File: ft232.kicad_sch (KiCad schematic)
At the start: 20 parts, among them J3 tp_ft232_, Q1 2N7002, U2 FT232BM

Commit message: Fix KiCad 10 footprint library: register kiC library, fix schematic references
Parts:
- J3: footprint Connector_Pin:pad_0508 -> kiC:pad_0508
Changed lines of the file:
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@@
 			)
 		)
-		(property "Footprint" "Connector_Pin:pad_0508"
+		(property "Footprint" "kiC:pad_0508"
 			(at 172.72 66.04 0)
 			(hide yes)

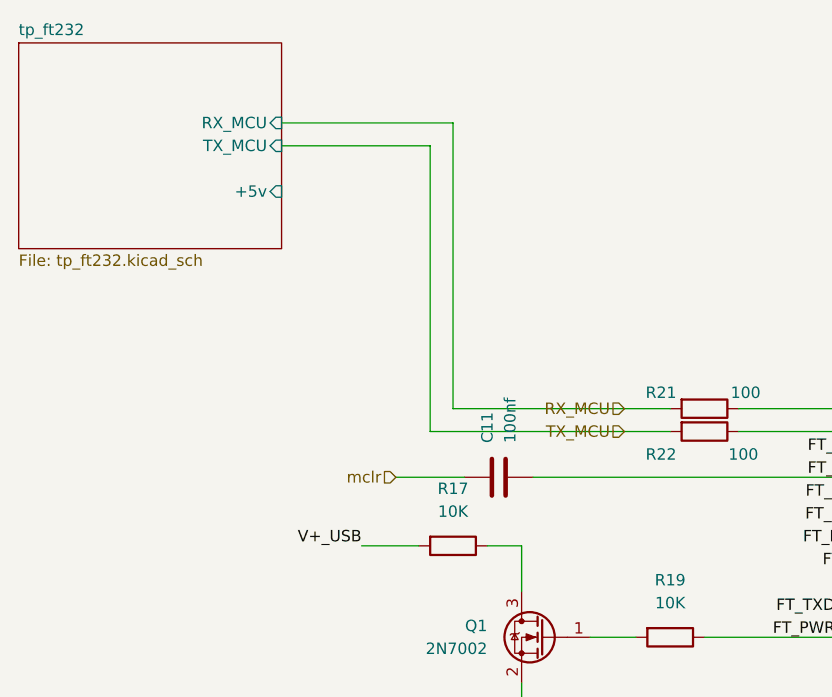
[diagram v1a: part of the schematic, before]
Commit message: feat: tp_ft232 hierarchical labels + ft232 sheet pins
- Convert 9 local labels in tp_ft232 to hierarchical labels
- Remove conflicting global labels (FT_CTS, FT_RTS)
- Add 9 sheet pins to tp_ft232 box in ft232.kicad_sch
- Restructure cnc-pic32 skill to .opencode/skills/cnc-pic32/SKILL.md
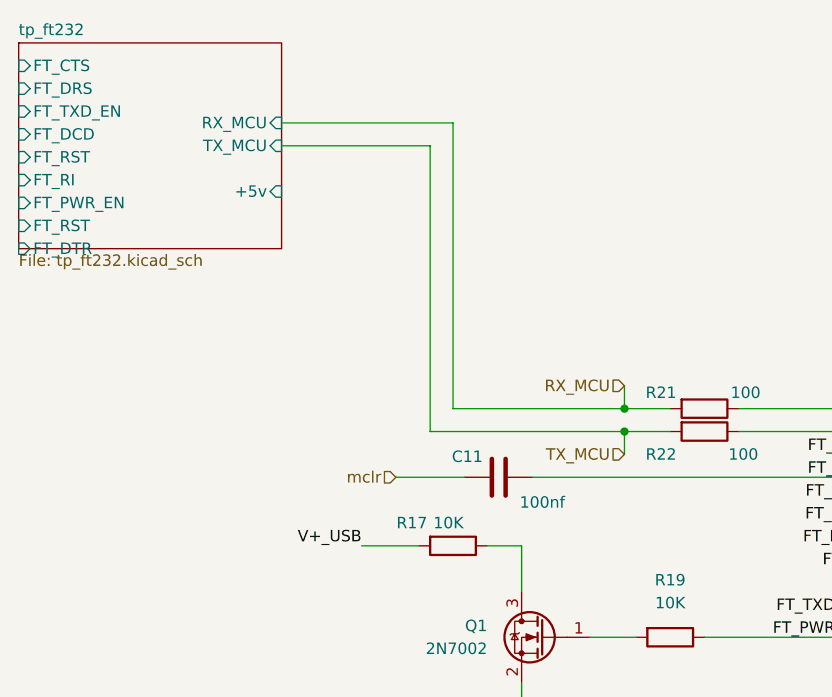
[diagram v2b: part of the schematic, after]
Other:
- sheet tp_ft232 ports: added FT_CTS, FT_DCD, FT_DRS, FT_DTR, FT_PWR_EN, FT_RI, FT_RST, FT_TXD_EN; removed none
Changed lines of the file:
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@@
 	(paper "A4")
 	(junction
+		(at 97.79 78.74)
+		(diameter 0)
+		(color 0 0 0 0)
+	)
+	(junction
 		(at 147.32 137.16)
 		(diameter 0)
@@
 	)
 	(junction
+		(at 97.79 81.28)
+		(diameter 0)
+		(color 0 0 0 0)
+	)
+	(junction
 		(at 180.34 66.04)
 		(diameter 0)
@@
 	(wire
 		(pts
+			(xy 97.79 76.2) (xy 97.79 78.74)
+		)
+		(stroke
+			(width 0)
+			(type default)
+		)
+	)
+	(wire
+		(pts
 			(xy 152.4 66.04) (xy 152.4 71.12)
 		)
@@
 	(wire
 		(pts
+			(xy 97.79 78.74) (xy 102.87 78.74)
+		)
+		(stroke
+			(width 0)
+			(type default)
+		)
+	)
+	(wire
+		(pts
 			(xy 196.85 106.68) (xy 198.12 106.68)
 		)
@@
 	(wire
 		(pts
-			(xy 78.74 78.74) (xy 102.87 78.74)
+			(xy 78.74 78.74) (xy 97.79 78.74)
 		)
 		(stroke
@@
 	(wire
 		(pts
-			(xy 76.2 81.28) (xy 102.87 81.28)
+			(xy 76.2 81.28) (xy 97.79 81.28)
 		)
 		(stroke
@@
 	(wire
 		(pts
+			(xy 97.79 81.28) (xy 102.87 81.28)
+		)
+		(stroke
+			(width 0)
+			(type default)
+		)
+	)
+	(wire
+		(pts
 			(xy 97.79 111.76) (xy 124.46 111.76)
 		)
@@
 	(wire
 		(pts
+			(xy 97.79 83.82) (xy 97.79 81.28)
+		)
+		(stroke
+			(width 0)
+			(type default)
+		)
+	)
+	(wire
+		(pts
 			(xy 97.79 116.84) (xy 97.79 111.76)
 		)
@@
 	(hierarchical_label "RX_MCU"
 		(shape input)
-		(at 97.79 78.74 180)
+		(at 97.79 76.2 180)
 		(effects
 			(font
@@
 	(hierarchical_label "TX_MCU"
 		(shape input)
-		(at 97.79 81.28 180)
+		(at 97.79 83.82 180)
 		(effects
 			(font
@@
 		(dnp no)
 		(property "Reference" "C11"
-			(at 82.55 82.55 0)
+			(at 82.042 84.074 90)
 			(show_name no)
 			(do_not_autoplace no)
@@
 		)
 		(property "Value" "100nf"
-			(at 85.09 82.55 0)
+			(at 91.186 89.154 90)
 			(show_name no)
 			(do_not_autoplace no)
@@
 		(in_pos_files yes)
 		(dnp no)
-		(fields_autoplaced yes)
 		(property "Reference" "R17"
-			(at 78.74 87.63 90)
+			(at 74.168 91.44 90)
 			(show_name no)
 			(do_not_autoplace no)
@@
 		)
 		(property "Value" "10K"
-			(at 78.74 90.17 90)
+			(at 78.232 91.44 90)
 			(show_name no)
 			(do_not_autoplace no)
@@
 			)
 		)
+		(pin "FT_CTS" input
+			(at 30.48 40.64 180)
+			(effects
+				(font
+					(size 1.27 1.27)
+				)
+				(justify left)
+			)
+		)
+		(pin "FT_DRS" input
+			(at 30.48 43.18 180)
+			(effects
+				(font
+					(size 1.27 1.27)
+				)
+				(justify left)
+			)
+		)
+		(pin "FT_TXD_EN" input
+			(at 30.48 45.72 180)
+			(effects
+				(font
+					(size 1.27 1.27)
+				)
+				(justify left)
+			)
+		)
+		(pin "FT_DCD" input
+			(at 30.48 48.26 180)
+			(effects
+				(font
+					(size 1.27 1.27)
+				)
+				(justify left)
+			)
+		)
+		(pin "FT_RST" input
+			(at 30.48 50.80 180)
+			(effects
+				(font
+					(size 1.27 1.27)
+				)
+				(justify left)
+			)
+		)
+		(pin "FT_RI" input
+			(at 30.48 53.34 180)
+			(effects
+				(font
+					(size 1.27 1.27)
+				)
+				(justify left)
+			)
+		)
+		(pin "FT_PWR_EN" input
+			(at 30.48 55.88 180)
+			(effects
+				(font
+					(size 1.27 1.27)
+				)
+				(justify left)
+			)
+		)
+		(pin "FT_RST" input
+			(at 30.48 58.42 180)
+			(effects
+				(font
+					(size 1.27 1.27)
+				)
+				(justify left)
+			)
+		)
+		(pin "FT_DTR" input
+			(at 30.48 60.96 180)
+			(effects
+				(font
+					(size 1.27 1.27)
+				)
+				(justify left)
+			)
+		)

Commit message: fix: tp_ft232 footprints kiC:pad_0508 + kiC:Pin_D1.5mmx1mm → Library:connector_pin1
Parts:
- J3: footprint kiC:pad_0508 -> Library:connector_pin1
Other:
- sheet power_ft232 ports: added FT_RESET; removed none
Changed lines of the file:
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@@
+	(wire
+		(pts
+			(xy 86.36 158.75) (xy 76.2 158.75)
+		)
+		(stroke
+			(width 0)
+			(type default)
+		)
+	)
 	(wire
 		(pts
@@
 			)
 			(justify right bottom)
+		)
+	)
+	(label "FT_RESET"
+		(at 86.36 158.75 0)
+		(effects
+			(font
+				(size 1.27 1.27)
+			)
+			(justify left bottom)
 		)
 	)
@@
 			)
 		)
-		(property "Footprint" "kiC:pad_0508"
+		(property "Footprint" "Library:connector_pin1"
 			(at 172.72 66.04 0)
 			(hide yes)
@@
 			)
 		)
+		(pin "FT_RESET" input
+			(at 76.2 158.75 0)
+			(effects
+				(font
+					(size 1.27 1.27)
+				)
+				(justify right)
+			)
+		)
 		(instances
 			(project "cnc_pic32"
@@
 		)
 		(pin "FT_RST" input
-			(at 30.48 50.80 180)
-			(effects
-				(font
+			(at 30.48 50.8 180)
+			(effects
+				(font

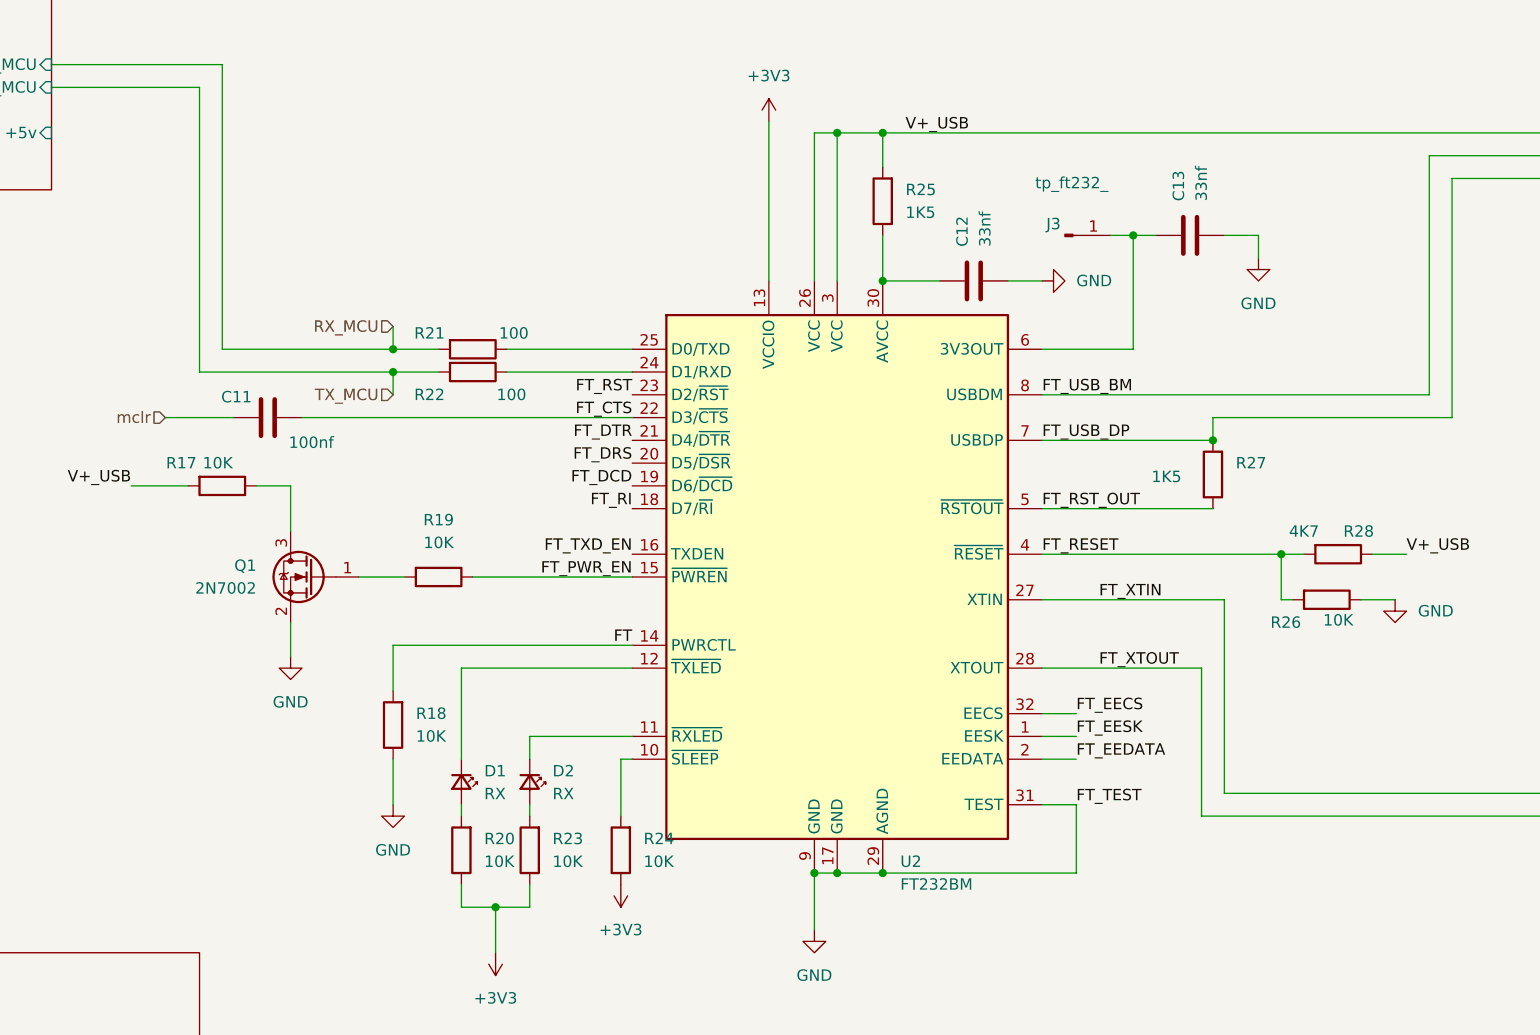
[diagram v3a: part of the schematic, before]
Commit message: feat: 25 hierarchical labels for 5 Pololus + fix J4/J15/J17/TP17 footprints + USB pin6→SH
- pololu.kicad_sch: 5→25 hierarchical labels (reset_N, sleep_N, enable_N, step_N, dir_N) with wires to each Pololu A4988
- pololu.kicad_sch: J17 footprint kiC:PinHeader → Library:PinHeader_1x06_P2.54mm_Vertical
- cnc_pic32.kicad_sch: expanded Pololu sheet box with 25 named sheet pins
- buttons.kicad_sch: all SW switches → Button_Switch_SMD:SW_SPST_CK_RS282G05A3
- tp_ft232.kicad_sch: kiC:pad_0508 + kiC:Pin_D1.5mmx1mm → Library:connector_pin1
- usb_conector_Ft232.kicad_sch: J4/J15 kiC:Pin_D1.5mmx1mm → Library:connector_pin1, J5 pin 6→SH
- Usb_pic32.kicad_sch: TP17 kiC:Pin_D1.5mmx1mm → Library:connector_pin1, J18 pin 6→SH
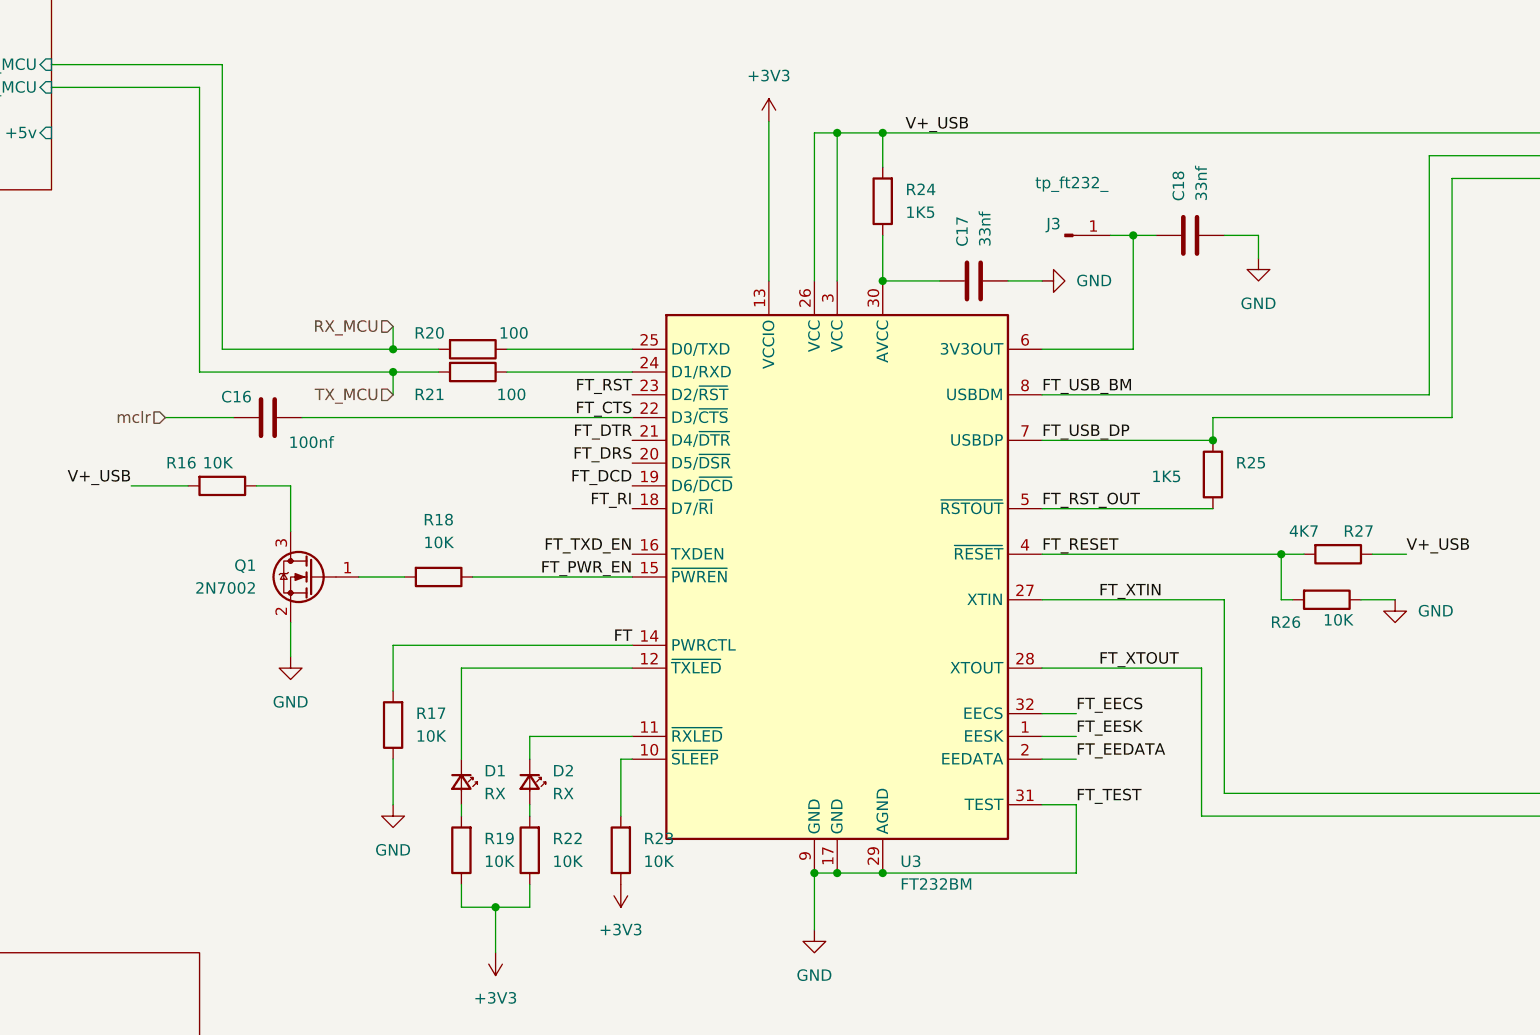
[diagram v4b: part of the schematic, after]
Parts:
- renumbered C11 to C16, C12 to C17, C13 to C18, R17 to R16, R18 to R17, R19 to R18, R20 to R19, R21 to R20, R22 to R21, R23 to R22, R24 to R23, R25 to R24, R27 to R25, R28 to R27, U2 to U3
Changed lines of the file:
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@@
 		(dnp no)
 		(fields_autoplaced yes)
-		(property "Reference" "#PWR07"
+		(property "Reference" "#PWR018"
 			(at 86.36 119.38 0)
 			(hide yes)
@@
 			(project "cnc_pic32"
 				(path "/13dbfc1f-be47-44ca-9042-3d6a9a657d7d/22a12b0c-67ed-4f76-a580-7ac736b63dbd"
-					(reference "#PWR07")
+					(reference "#PWR018")
 					(unit 1)
 				)
@@
 		(dnp no)
 		(fields_autoplaced yes)
-		(property "Reference" "U2"
+		(property "Reference" "U3"
 			(at 154.3559 135.89 0)
 			(show_name no)
@@
 			(project "cnc_pic32"
 				(path "/13dbfc1f-be47-44ca-9042-3d6a9a657d7d/22a12b0c-67ed-4f76-a580-7ac736b63dbd"
-					(reference "U2")
+					(reference "U3")
 					(unit 1)
 				)
@@
 		(in_pos_files yes)
 		(dnp no)
-		(property "Reference" "C13"
+		(property "Reference" "C18"
 			(at 185.42 62.23 0)
 			(show_name no)
@@
 			(project "cnc_pic32"
 				(path "/13dbfc1f-be47-44ca-9042-3d6a9a657d7d/22a12b0c-67ed-4f76-a580-7ac736b63dbd"
-					(reference "C13")
+					(reference "C18")
 					(unit 1)
 				)
@@
 		(dnp no)
 		(fields_autoplaced yes)
-		(property "Reference" "#PWR014"
+		(property "Reference" "#PWR026"
 			(at 209.55 113.03 0)
 			(hide yes)
@@
 			(project "cnc_pic32"
 				(path "/13dbfc1f-be47-44ca-9042-3d6a9a657d7d/22a12b0c-67ed-4f76-a580-7ac736b63dbd"
-					(reference "#PWR014")
+					(reference "#PWR026")
 					(unit 1)
 				)
@@
 		(dnp no)
 		(fields_autoplaced yes)
-		(property "Reference" "#PWR010"
+		(property "Reference" "#PWR021"
 			(at 123.19 134.62 0)
 			(hide yes)
@@
 			(project "cnc_pic32"
 				(path "/13dbfc1f-be47-44ca-9042-3d6a9a657d7d/22a12b0c-67ed-4f76-a580-7ac736b63dbd"
-					(reference "#PWR010")
+					(reference "#PWR021")
 					(unit 1)
 				)
@@
 		(dnp no)
 		(fields_autoplaced yes)
-		(property "Reference" "#PWR015"
+		(property "Reference" "#PWR025"
 			(at 194.31 74.93 0)
 			(hide yes)
@@
 			(project "cnc_pic32"
 				(path "/13dbfc1f-be47-44ca-9042-3d6a9a657d7d/22a12b0c-67ed-4f76-a580-7ac736b63dbd"
-					(reference "#PWR015")
+					(reference "#PWR025")
 					(unit 1)
 				)
@@
 		(dnp no)
 		(fields_autoplaced yes)
-		(property "Reference" "R19"
+		(property "Reference" "R18"
 			(at 102.87 97.79 90)
 			(show_name no)
@@
 			(project "cnc_pic32"
 				(path "/13dbfc1f-be47-44ca-9042-3d6a9a657d7d/22a12b0c-67ed-4f76-a580-7ac736b63dbd"
-					(reference "R19")
+					(reference "R18")
 					(unit 1)
 				)
@@
 		(dnp no)
 		(fields_autoplaced yes)
-		(property "Reference" "R18"
+		(property "Reference" "R17"
 			(at 100.33 119.38 0)
 			(show_name no)
@@
 			(project "cnc_pic32"
 				(path "/13dbfc1f-be47-44ca-9042-3d6a9a657d7d/22a12b0c-67ed-4f76-a580-7ac736b63dbd"
-					(reference "R18")
+					(reference "R17")
 					(unit 1)
 				)
@@
 		(dnp no)
 		(fields_autoplaced yes)
-		(property "Reference" "R25"
+		(property "Reference" "R24"
 			(at 154.94 60.96 0)
 			(show_name no)
@@
 			(project "cnc_pic32"
 				(path "/13dbfc1f-be47-44ca-9042-3d6a9a657d7d/22a12b0c-67ed-4f76-a580-7ac736b63dbd"
-					(reference "R25")
+					(reference "R24")
 					(unit 1)
 				)
@@
 		(in_pos_files yes)
 		(dnp no)
-		(property "Reference" "R21"
+		(property "Reference" "R20"
 			(at 101.854 76.962 90)
 			(show_name no)
@@
 			(project "cnc_pic32"
 				(path "/13dbfc1f-be47-44ca-9042-3d6a9a657d7d/22a12b0c-67ed-4f76-a580-7ac736b63dbd"
-					(reference "R21")
+					(reference "R20")
 					(unit 1)
 				)
@@
 		(dnp no)
 		(fields_autoplaced yes)
-		(property "Reference" "R24"
+		(property "Reference" "R23"
 			(at 125.73 133.35 0)
 			(show_name no)
@@
 			(project "cnc_pic32"
 				(path "/13dbfc1f-be47-44ca-9042-3d6a9a657d7d/22a12b0c-67ed-4f76-a580-7ac736b63dbd"
-					(reference "R24")
+					(reference "R23")
 					(unit 1)
 				)
@@
 		(in_pos_files yes)
 		(dnp no)
-		(property "Reference" "C11"
+		(property "Reference" "C16"
 			(at 82.042 84.074 90)
 			(show_name no)
@@
 			(project "cnc_pic32"
 				(path "/13dbfc1f-be47-44ca-9042-3d6a9a657d7d/22a12b0c-67ed-4f76-a580-7ac736b63dbd"
-					(reference "C11")
+					(reference "C16")
 					(unit 1)
 				)
@@
 		(in_pos_files yes)
 		(dnp no)
-		(property "Reference" "R28"
+		(property "Reference" "R27"
 			(at 205.486 99.06 90)
 			(show_name no)
@@
 			(project "cnc_pic32"
 				(path "/13dbfc1f-be47-44ca-9042-3d6a9a657d7d/22a12b0c-67ed-4f76-a580-7ac736b63dbd"
-					(reference "R28")
+					(reference "R27")
 					(unit 1)
 				)
@@
 		(in_pos_files yes)
 		(dnp no)
-		(property "Reference" "R17"
+		(property "Reference" "R16"
 			(at 74.168 91.44 90)
 			(show_name no)
@@
 			(project "cnc_pic32"
 				(path "/13dbfc1f-be47-44ca-9042-3d6a9a657d7d/22a12b0c-67ed-4f76-a580-7ac736b63dbd"
-					(reference "R17")
+					(reference "R16")
 					(unit 1)
 				)
@@
 		(in_pos_files yes)
 		(dnp no)
-		(property "Reference" "C12"
+		(property "Reference" "C17"
 			(at 161.29 67.31 0)
 			(show_name no)
@@
 			(project "cnc_pic32"
 				(path "/13dbfc1f-be47-44ca-9042-3d6a9a657d7d/22a12b0c-67ed-4f76-a580-7ac736b63dbd"
-					(reference "C12")
+					(reference "C17")
 					(unit 1)
 				)
@@
 		(dnp no)
 		(fields_autoplaced yes)
-		(property "Reference" "#PWR011"
+		(property "Reference" "#PWR022"
 			(at 139.7 57.15 0)
 			(hide yes)
@@
 			(project "cnc_pic32"
 				(path "/13dbfc1f-be47-44ca-9042-3d6a9a657d7d/22a12b0c-67ed-4f76-a580-7ac736b63dbd"
-					(reference "#PWR011")
+					(reference "#PWR022")
 					(unit 1)
 				)
@@
 		(dnp no)
 		(fields_autoplaced yes)
-		(property "Reference" "R23"
+		(property "Reference" "R22"
 			(at 115.57 133.35 0)
 			(show_name no)
@@
 			(project "cnc_pic32"
 				(path "/13dbfc1f-be47-44ca-9042-3d6a9a657d7d/22a12b0c-67ed-4f76-a580-7ac736b63dbd"
-					(reference "R23")
+					(reference "R22")
 					(unit 1)
 				)
@@
 		(in_pos_files yes)
 		(dnp no)
-		(property "Reference" "R27"
+		(property "Reference" "R25"
 			(at 191.77 91.44 0)
 			(show_name no)
@@
 			(project "cnc_pic32"
 				(path "/13dbfc1f-be47-44ca-9042-3d6a9a657d7d/22a12b0c-67ed-4f76-a580-7ac736b63dbd"
-					(reference "R27")
+					(reference "R25")
 					(unit 1)
 				)
@@
 		(dnp no)
 		(fields_autoplaced yes)
-		(property "Reference" "#PWR012"
+		(property "Reference" "#PWR023"
 			(at 144.78 149.86 0)
 			(hide yes)
@@
 			(project "cnc_pic32"
 				(path "/13dbfc1f-be47-44ca-9042-3d6a9a657d7d/22a12b0c-67ed-4f76-a580-7ac736b63dbd"
-					(reference "#PWR012")
+					(reference "#PWR023")
 					(unit 1)
 				)
@@
 		(dnp no)
 		(fields_autoplaced yes)
-		(property "Reference" "#PWR08"
+		(property "Reference" "#PWR019"
 			(at 97.79 135.89 0)
 			(hide yes)
@@
 			(project "cnc_pic32"
 				(path "/13dbfc1f-be47-44ca-9042-3d6a9a657d7d/22a12b0c-67ed-4f76-a580-7ac736b63dbd"
-					(reference "#PWR08")
+					(reference "#PWR019")
 					(unit 1)
 				)
@@
 		(in_pos_files yes)
 		(dnp no)
-		(property "Reference" "R22"
+		(property "Reference" "R21"
 			(at 101.854 83.82 90)
 			(show_name no)
@@
 			(project "cnc_pic32"
 				(path "/13dbfc1f-be47-44ca-9042-3d6a9a657d7d/22a12b0c-67ed-4f76-a580-7ac736b63dbd"
-					(reference "R22")
+					(reference "R21")
 					(unit 1)
 				)
@@
 		(dnp no)
 		(fields_autoplaced yes)
-		(property "Reference" "#PWR013"
+		(property "Reference" "#PWR024"
 			(at 176.53 71.12 0)
 			(hide yes)
@@
 			(project "cnc_pic32"
 				(path "/13dbfc1f-be47-44ca-9042-3d6a9a657d7d/22a12b0c-67ed-4f76-a580-7ac736b63dbd"
-					(reference "#PWR013")
+					(reference "#PWR024")
 					(unit 1)
 				)
@@
 		(dnp no)
 		(fields_autoplaced yes)
-		(property "Reference" "#PWR09"
+		(property "Reference" "#PWR020"
 			(at 109.22 142.24 0)
 			(hide yes)
@@
 			(project "cnc_pic32"
 				(path "/13dbfc1f-be47-44ca-9042-3d6a9a657d7d/22a12b0c-67ed-4f76-a580-7ac736b63dbd"
-					(reference "#PWR09")
+					(reference "#PWR020")
 					(unit 1)
 				)
@@
 		(dnp no)
 		(fields_autoplaced yes)
-		(property "Reference" "R20"
+		(property "Reference" "R19"
 			(at 107.95 133.35 0)
 			(show_name no)
@@
 			(project "cnc_pic32"
 				(path "/13dbfc1f-be47-44ca-9042-3d6a9a657d7d/22a12b0c-67ed-4f76-a580-7ac736b63dbd"
-					(reference "R20")
-					(unit 1)
-				)
+					(reference "R19")
+					(unit 1)
+				)
